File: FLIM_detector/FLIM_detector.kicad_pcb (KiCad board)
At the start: 2 copper layers, 7 parts, among them U1 OPA858xDSG, U2 LM4040DBZ-2.0

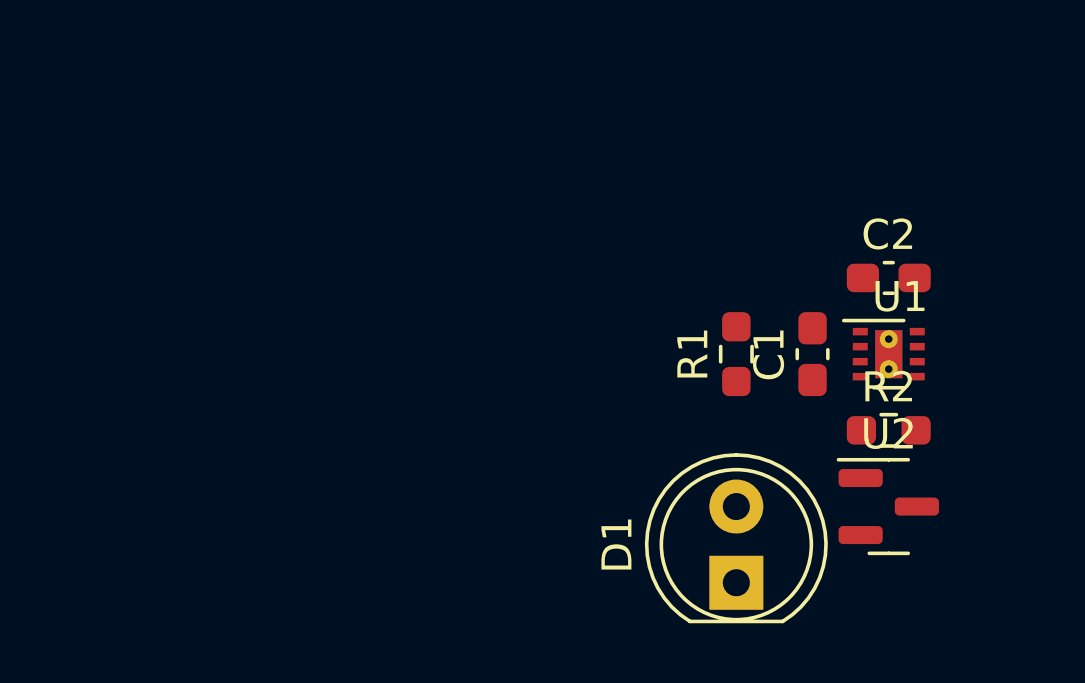
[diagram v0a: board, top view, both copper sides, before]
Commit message: v0.3 power source waas added, some components were decreased into 0402
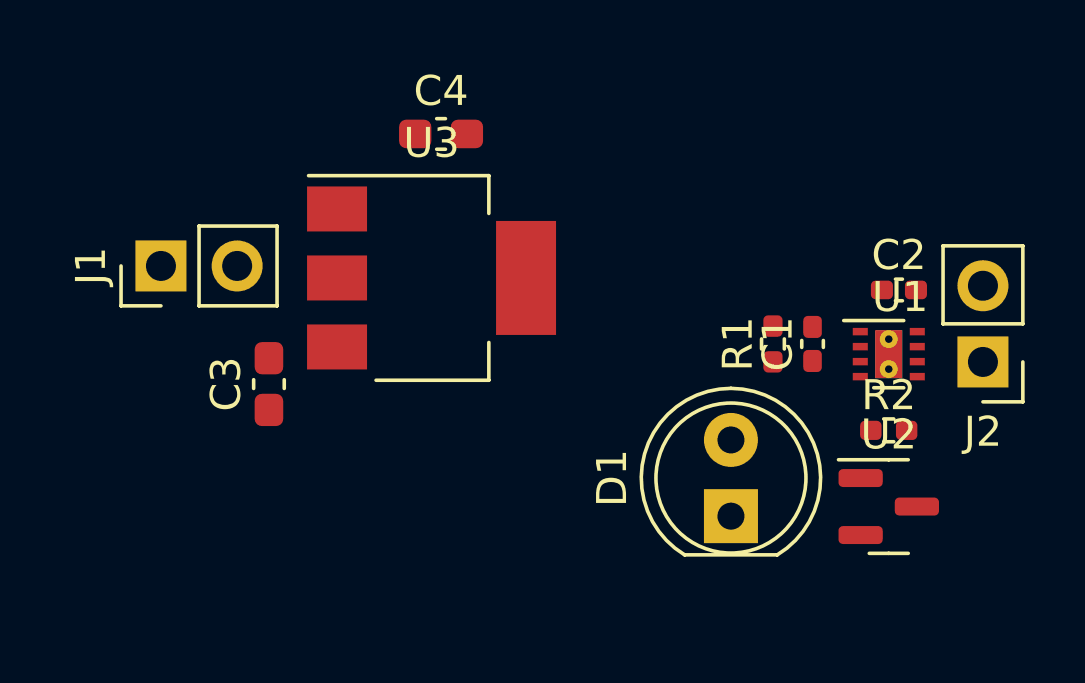
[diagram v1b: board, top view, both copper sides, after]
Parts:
- added C3: C, Capacitor_SMD:C_0603_1608Metric_Pad1.08x0.95mm_HandSolder, F.Cu at (230.8, 28.9)
- added C4: C, Capacitor_SMD:C_0603_1608Metric_Pad1.08x0.95mm_HandSolder, F.Cu at (236.5, 20.6)
- added J1: Conn_01x02_Female, Connector_PinHeader_2.54mm:PinHeader_1x02_P2.54mm_Vertical, F.Cu at (227.2, 25.0)
- added J2: Conn_01x02_Female, Connector_PinHeader_2.54mm:PinHeader_1x02_P2.54mm_Vertical, F.Cu at (254.6, 28.2)
- added U3: AMS1117-5.0, Package_TO_SOT_SMD:SOT-223-3_TabPin2, F.Cu at (236.2, 25.4)
- C1, C2: footprint Capacitor_SMD:C_0603_1608Metric_Pad1.08x0.95mm_HandSolder -> Capacitor_SMD:C_0402_1005Metric_Pad0.74x0.62mm_HandSolder
- R1, R2: footprint Resistor_SMD:R_0603_1608Metric_Pad0.98x0.95mm_HandSolder -> Resistor_SMD:R_0402_1005Metric_Pad0.72x0.64mm_HandSolder
- moved D1 2.23 mm to (246.2, 33.3)
- moved R1 1.27 mm to (247.6, 27.6)
- moved C2 0.52 mm to (251.8, 25.8)
- moved C1 0.34 mm to (248.9, 27.6)

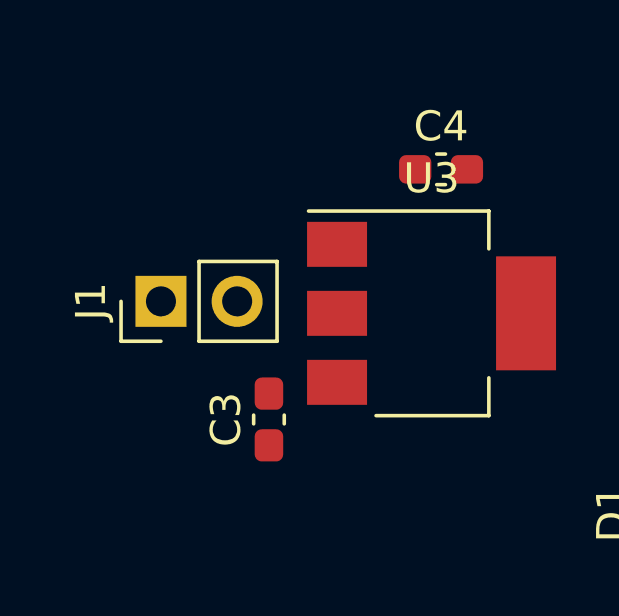
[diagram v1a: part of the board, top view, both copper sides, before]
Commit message: v0.4 input shotthy was added
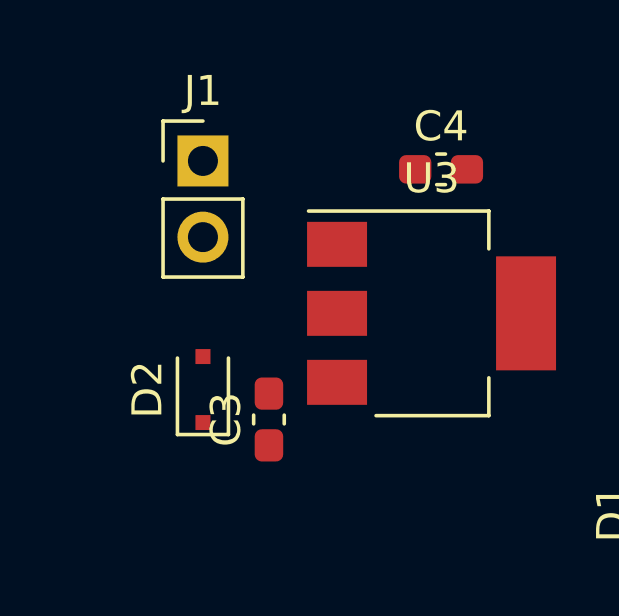
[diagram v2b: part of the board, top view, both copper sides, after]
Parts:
- added D2: PMEG4010CEJ, Diode_SMD:D_SOD-323F, F.Cu at (228.6, 27.9)
- moved J1 4.88 mm to (228.6, 20.3), turned to 0 degrees
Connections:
- J1 pad 2: Net-(C3-Pad2) -> Net-(J1-Pad2)
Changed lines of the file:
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@@
   (net 7 "Net-(C3-Pad2)")
   (net 8 "Net-(J2-Pad1)")
+  (net 9 "Net-(J1-Pad2)")
   (footprint "Resistor_SMD:R_0402_1005Metric_Pad0.72x0.64mm_HandSolder" (layer "F.Cu")
     (at 247.6 27.6 90)
@@
     )
   )
+  (footprint "Diode_SMD:D_SOD-323F" (layer "F.Cu")
+    (at 228.6 27.94 90)
+    (descr "SOD-323F http://www.nxp.com/documents/outline_drawing/SOD323F.pdf")
+    (tags "SOD-323F")
+    (property "Sheetfile" "FLIM_detector.kicad_sch")
+    (property "Sheetname" "")
+    (attr smd)
+    (fp_text reference "D2" (at 0 -1.85 90) (layer "F.SilkS")
+      (effects (font (size 1 1) (thickness 0.15)))
+    )
+    (fp_text value "PMEG4010CEJ" (at 0.1 1.9 90) (layer "F.Fab")
+      (effects (font (size 1 1) (thickness 0.15)))
+    )
+    (fp_text user "${REFERENCE}" (at 0 -1.85 90) (layer "F.Fab")
+      (effects (font (size 1 1) (thickness 0.15)))
+    )
+    (fp_line (start -1.5 0.85) (end 1.05 0.85) (layer "F.SilkS") (width 0.12))
+    (fp_line (start -1.5 -0.85) (end -1.5 0.85) (layer "F.SilkS") (width 0.12))
+    (fp_line (start -1.5 -0.85) (end 1.05 -0.85) (layer "F.SilkS") (width 0.12))
+    (fp_line (start 1.6 -0.95) (end 1.6 0.95) (layer "F.CrtYd") (width 0.05))
+    (fp_line (start -1.6 -0.95) (end 1.6 -0.95) (layer "F.CrtYd") (width 0.05))
+    (fp_line (start -1.6 0.95) (end 1.6 0.95) (layer "F.CrtYd") (width 0.05))
+    (fp_line (start -1.6 -0.95) (end -1.6 0.95) (layer "F.CrtYd") (width 0.05))
+    (fp_line (start 0.2 -0.35) (end 0.2 0.35) (layer "F.Fab") (width 0.1))
+    (fp_line (start -0.3 -0.35) (end -0.3 0.35) (layer "F.Fab") (width 0.1))
+    (fp_line (start -0.3 0) (end 0.2 -0.35) (layer "F.Fab") (width 0.1))
+    (fp_line (start 0.2 0.35) (end -0.3 0) (layer "F.Fab") (width 0.1))
+    (fp_line (start 0.9 -0.7) (end 0.9 0.7) (layer "F.Fab") (width 0.1))
+    (fp_line (start -0.9 0.7) (end -0.9 -0.7) (layer "F.Fab") (width 0.1))
+    (fp_line (start 0.2 0) (end 0.45 0) (layer "F.Fab") (width 0.1))
+    (fp_line (start -0.3 0) (end -0.5 0) (layer "F.Fab") (width 0.1))
+    (fp_line (start 0.9 0.7) (end -0.9 0.7) (layer "F.Fab") (width 0.1))
+    (fp_line (start -0.9 -0.7) (end 0.9 -0.7) (layer "F.Fab") (width 0.1))
+    (pad "1" smd rect (at -1.1 0 90) (size 0.5 0.5) (layers "F.Cu" "F.Paste" "F.Mask")
+      (net 7 "Net-(C3-Pad2)") (pinfunction "K") (pintype "passive"))
+    (pad "2" smd rect (at 1.1 0 90) (size 0.5 0.5) (layers "F.Cu" "F.Paste" "F.Mask")
+      (net 9 "Net-(J1-Pad2)") (pinfunction "A") (pintype "passive"))
+    (model "${KICAD6_3DMODEL_DIR}/Diode_SMD.3dshapes/D_SOD-323F.wrl"
+      (offset (xyz 0 0 0))
+      (scale (xyz 1 1 1))
+      (rotate (xyz 0 0 0))
+    )
+  )
   (footprint "Capacitor_SMD:C_0402_1005Metric_Pad0.74x0.62mm_HandSolder" (layer "F.Cu")
     (at 248.92 27.6 90)
@@
   )
   (footprint "Connector_PinHeader_2.54mm:PinHeader_1x02_P2.54mm_Vertical" (layer "F.Cu")
-    (at 227.2 25 90)
+    (at 228.6 20.32)
     (descr "Through hole straight pin header, 1x02, 2.54mm pitch, single row")
     (tags "Through hole pin header THT 1x02 2.54mm single row")
@@
     (property "Sheetname" "")
     (attr through_hole)
-    (fp_text reference "J1" (at 0 -2.33 90) (layer "F.SilkS")
-      (effects (font (size 1 1) (thickness 0.15)))
-    )
-    (fp_text value "Conn_01x02_Female" (at 0 4.87 90) (layer "F.Fab")
-      (effects (font (size 1 1) (thickness 0.15)))
-    )
-    (fp_text user "${REFERENCE}" (at 1.27 -1.27) (layer "F.Fab")
+    (fp_text reference "J1" (at 0 -2.33) (layer "F.SilkS")
+      (effects (font (size 1 1) (thickness 0.15)))
+    )
+    (fp_text value "Conn_01x02_Female" (at 0 4.87) (layer "F.Fab")
+      (effects (font (size 1 1) (thickness 0.15)))
+    )
+    (fp_text user "${REFERENCE}" (at 1.27 -1.27 90) (layer "F.Fab")
       (effects (font (size 1 1) (thickness 0.15)))
     )
@@
     (fp_line (start -1.27 3.81) (end -1.27 -0.635) (layer "F.Fab") (width 0.1))
     (fp_line (start -1.27 -0.635) (end -0.635 -1.27) (layer "F.Fab") (width 0.1))
-    (pad "1" thru_hole rect (at 0 0 90) (size 1.7 1.7) (drill 1) (layers *.Cu *.Mask)
+    (pad "1" thru_hole rect (at 0 0) (size 1.7 1.7) (drill 1) (layers *.Cu *.Mask)
       (net 3 "GND") (pinfunction "Pin_1") (pintype "passive"))
-    (pad "2" thru_hole oval (at 0 2.54 90) (size 1.7 1.7) (drill 1) (layers *.Cu *.Mask)
-      (net 7 "Net-(C3-Pad2)") (pinfunction "Pin_2") (pintype "passive"))
+    (pad "2" thru_hole oval (at 0 2.54) (size 1.7 1.7) (drill 1) (layers *.Cu *.Mask)
+      (net 9 "Net-(J1-Pad2)") (pinfunction "Pin_2") (pintype "passive"))
     (model "${KICAD6_3DMODEL_DIR}/Connector_PinHeader_2.54mm.3dshapes/PinHeader_1x02_P2.54mm_Vertical.wrl"
       (offset (xyz 0 0 0))

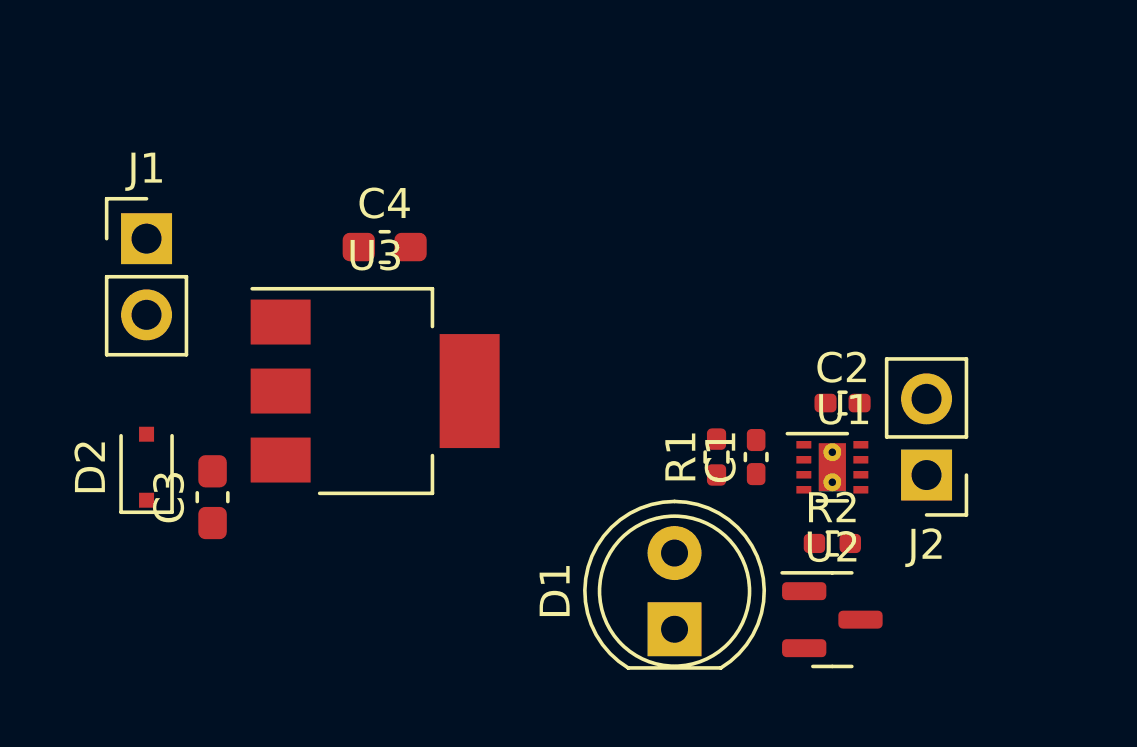
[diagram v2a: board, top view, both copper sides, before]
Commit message: v0.5 routing, polygons and mounting holes were added
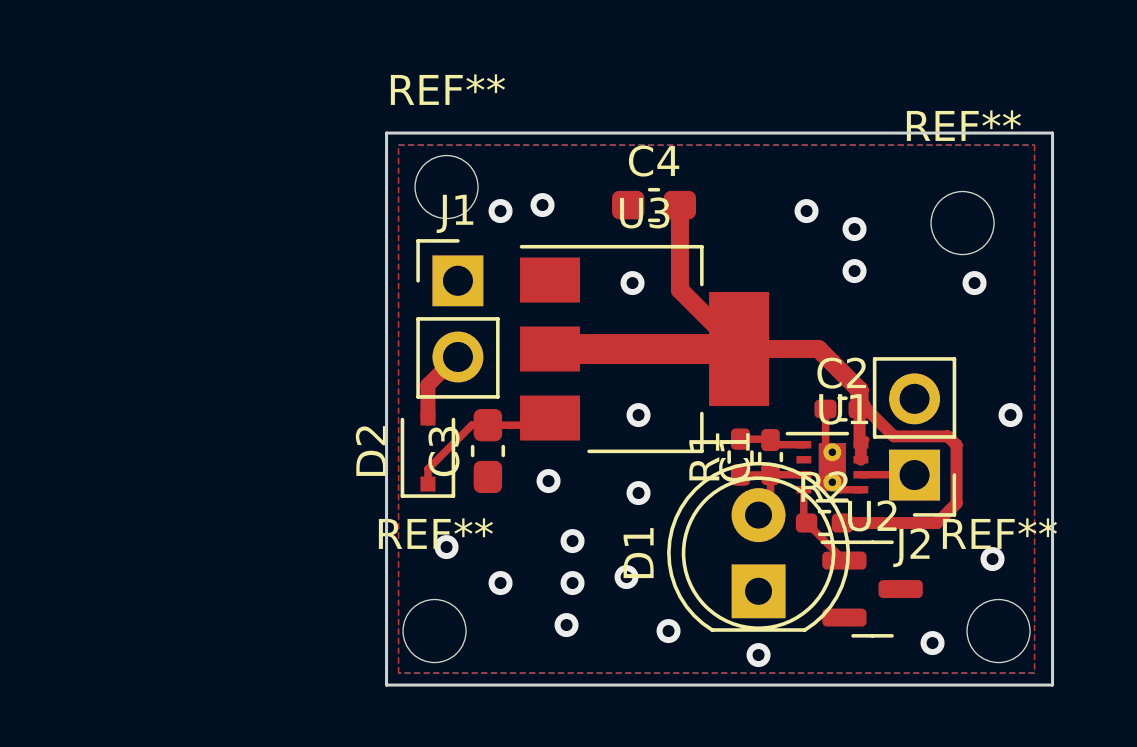
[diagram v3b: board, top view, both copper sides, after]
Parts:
- added REF**: MountingHole_2.1mm, MountingHole:MountingHole_2.1mm, F.Cu at (238.6, 18.6)
- added REF**: MountingHole_2.1mm, MountingHole:MountingHole_2.1mm, F.Cu at (257.0, 33.4)
- added REF**: MountingHole_2.1mm, MountingHole:MountingHole_2.1mm, F.Cu at (238.2, 33.4)
- added REF**: MountingHole_2.1mm, MountingHole:MountingHole_2.1mm, F.Cu at (255.8, 19.8)
- moved J1 10.5 mm to (239.0, 21.7)
- moved D2 9.40 mm to (238.0, 27.4)
- moved C3 9.31 mm to (240.0, 27.4)
- moved C4 9.09 mm to (245.5, 19.2)
- moved U3 9.09 mm to (245.2, 24.0)
- moved D1 3.07 mm to (249.0, 32.1)
- moved U2 1.68 mm to (252.8, 32.0)
- moved R1 0.80 mm to (248.4, 27.6)
- moved R2 0.73 mm to (251.2, 29.8)
- moved C1 0.48 mm to (249.4, 27.6)
- moved J2 0.40 mm to (254.2, 28.2)
- moved C2 0.20 mm to (251.8, 26.0)
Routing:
- net +5V: track 0.00 -> 28.8 mm
- net Net-(C3-Pad2): track 0.00 -> 5.27 mm
- net Net-(C1-Pad1): track 0.00 -> 3.70 mm
- net Net-(R2-Pad1): track 0.00 -> 2.93 mm
- net GND: track 0.00 -> 2.59 mm, vias 0 -> 21
- net Net-(J1-Pad2): track 0.00 -> 2.49 mm
- net Net-(C1-Pad2): track 0.00 -> 2.19 mm
- net Net-(J2-Pad1): track 0.00 -> 1.79 mm
- added copper zone on B.Cu, net GND
- added copper zone on F.Cu, net GND
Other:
- board outline added: 22.2 x 18.4 mm

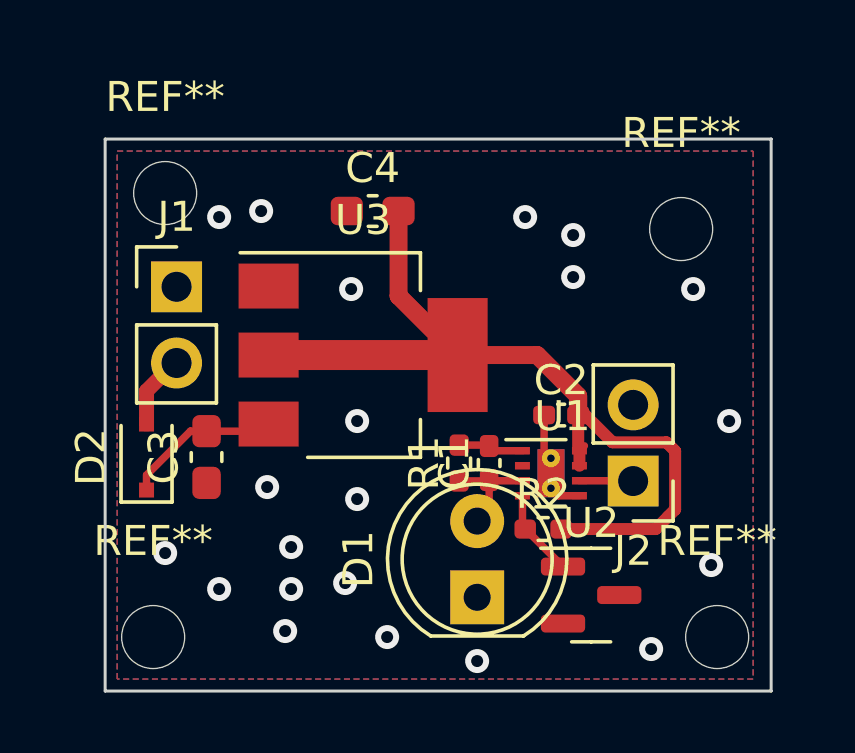
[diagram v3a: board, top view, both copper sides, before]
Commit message: v0.6 PCB size was decreased
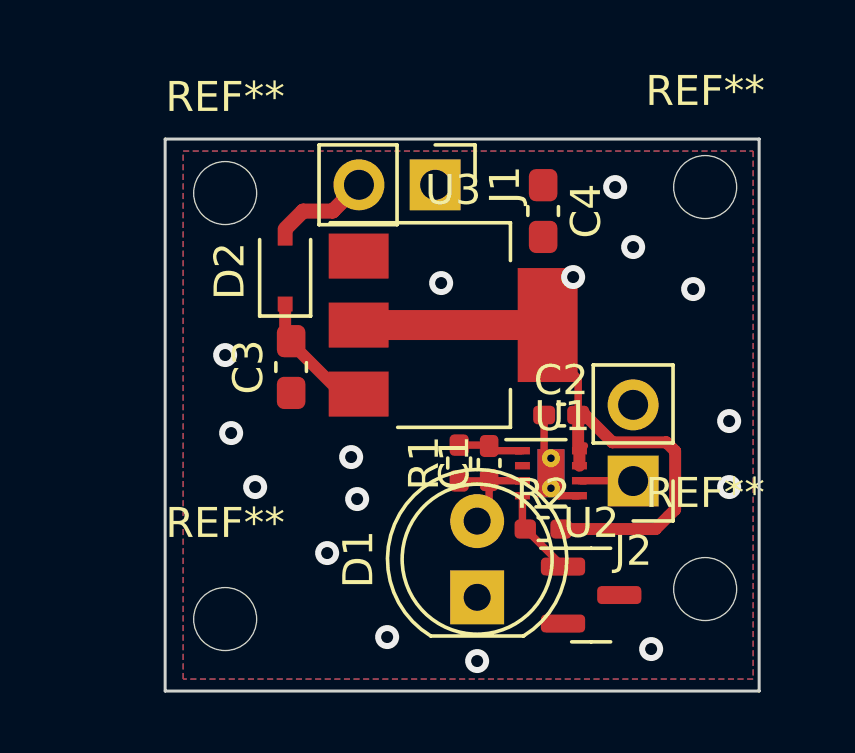
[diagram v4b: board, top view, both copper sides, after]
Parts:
- moved J1 9.27 mm to (247.6, 18.3), turned to -90 degrees
- moved D2 7.73 mm to (242.6, 21.2)
- moved C4 5.68 mm to (251.2, 19.2), turned to -90 degrees
- moved C3 4.12 mm to (242.8, 24.4)
- moved U3 3.16 mm to (248.2, 23.0)
- moved REF** 2.47 mm to (240.6, 32.8)
- moved REF** 2.00 mm to (240.6, 18.6)
- moved REF** 1.65 mm to (256.6, 31.8)
- moved REF** 1.61 mm to (256.6, 18.4)
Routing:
- net +5V: track 28.8 -> 21.4 mm
- net Net-(J1-Pad2): track 2.49 -> 3.37 mm
- net Net-(C3-Pad2): track 5.27 -> 4.67 mm
- net GND: vias 21 -> 16
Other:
- board size 22.2 x 18.4 mm -> 19.8 x 18.4 mm
